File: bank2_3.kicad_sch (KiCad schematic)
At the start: 5 parts, among them IC1 ECP5-BGA256

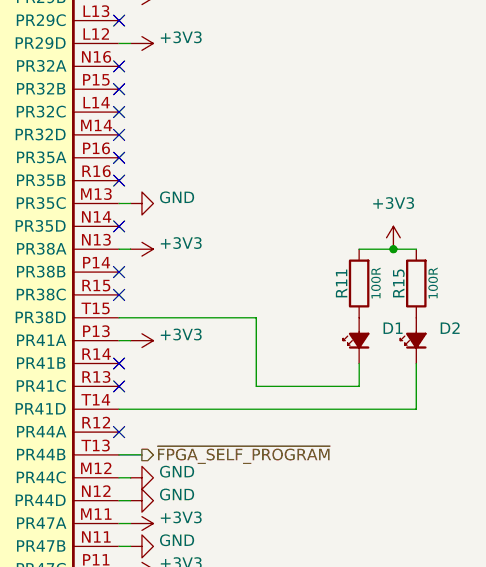
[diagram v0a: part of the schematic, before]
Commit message: kicad: fix LED PD, APMem, 1V8, USB ~RST short
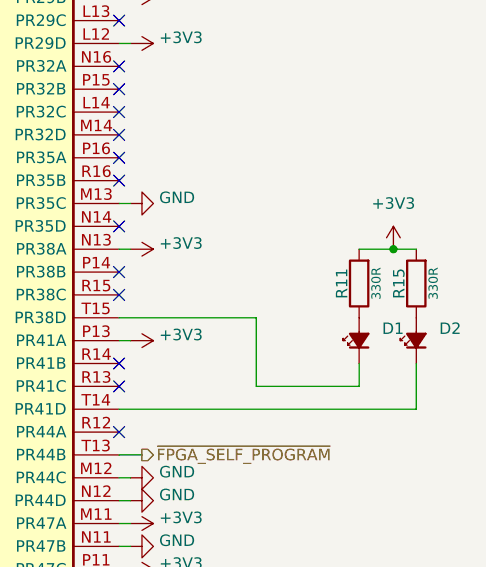
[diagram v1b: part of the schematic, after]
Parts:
- R11, R15: value 100R -> 330R; lcsc# C25076 -> C25104
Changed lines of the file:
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@@
 			)
 		)
-		(property "Value" "100R"
+		(property "Value" "330R"
 			(at 240.665 107.95 0)
 			(effects
@@
 			)
 		)
-		(property "lcsc#" "C25076"
+		(property "lcsc#" "C25104"
 			(at 238.76 107.95 0)
 			(effects
@@
 			)
 		)
-		(property "Value" "100R"
+		(property "Value" "330R"
 			(at 234.315 107.95 0)
 			(effects
@@
 			)
 		)
-		(property "lcsc#" "C25076"
+		(property "lcsc#" "C25104"
 			(at 232.41 107.95 0)
 			(effects
